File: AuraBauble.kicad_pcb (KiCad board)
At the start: 2 copper layers, 15 x 19 mm, 36 parts, among them J1 Bauble-Expando!, J2 USB_A, J3 SWD, SW1 KXT 321 LHS, U1 ATSAMD11D14A-M, U2 LP5912-3.3DRV, U3 74LVC1G02SE-7, Y1 FC-135R

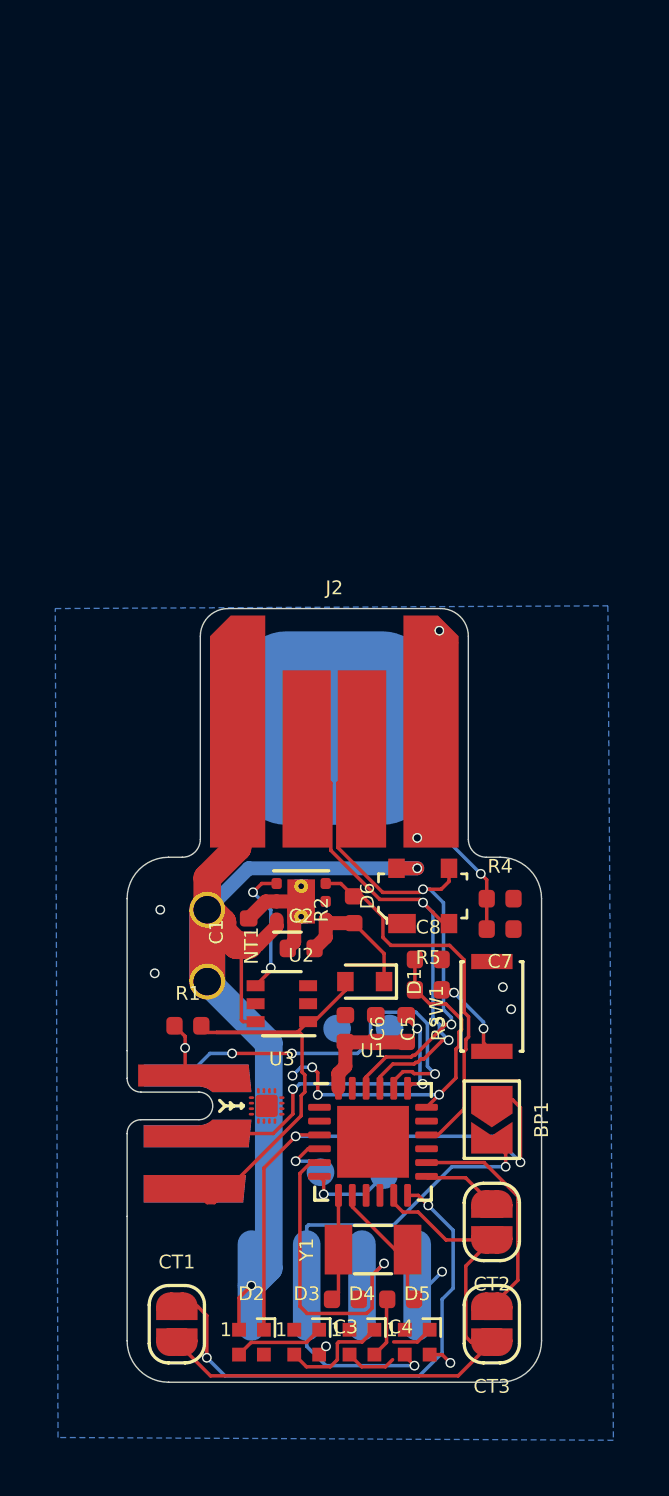
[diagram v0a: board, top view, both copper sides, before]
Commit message: Closing in on a rev0.
I still think I need to level shift the SPI signals to the LEDs.
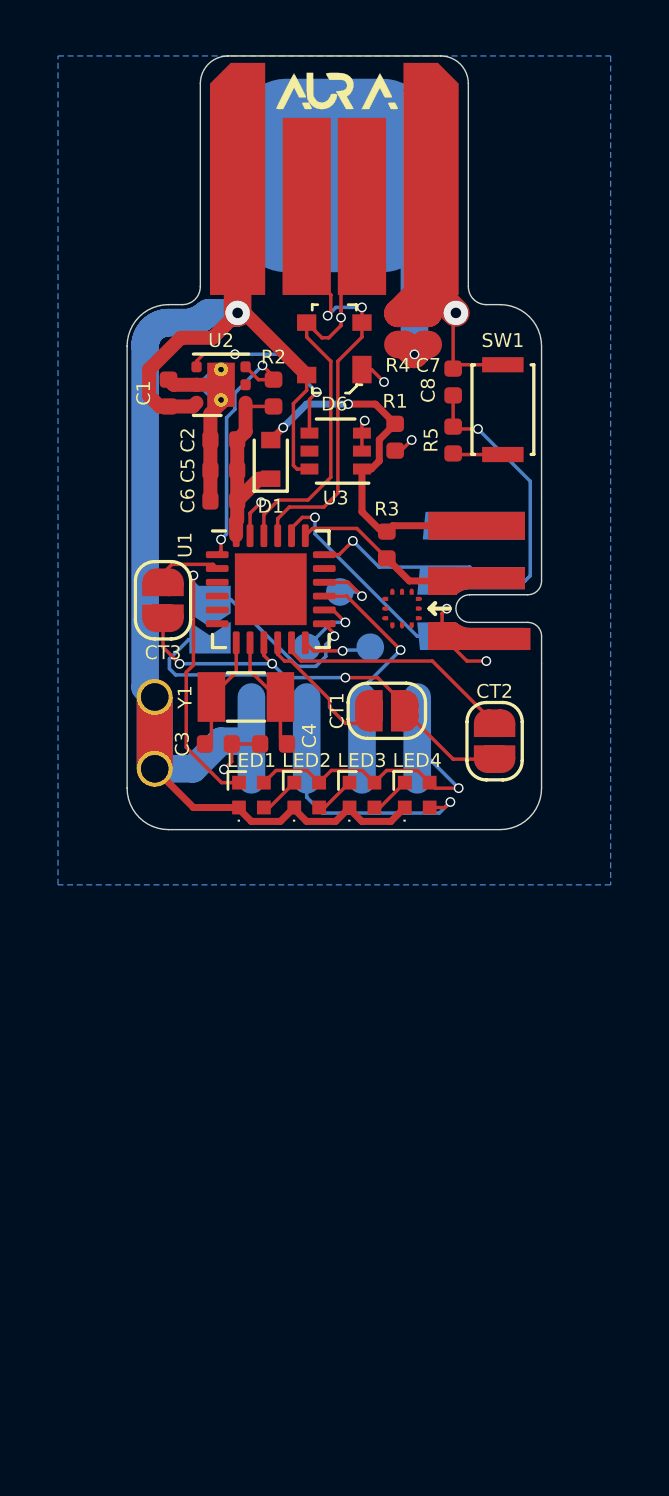
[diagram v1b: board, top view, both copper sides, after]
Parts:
- removed D2, D3, D4, D5: SK6805, LED_SMD:LED_SK6812_EC15_1.5x1.5mm
- removed TP4: TestPoint_Small, TestPoint:TestPoint_Pad_D1.0mm
- added LED1: SK6805, LED_SMD:LED_SK6812_EC15_1.5x1.5mm, F.Cu at (147.0, 76.8)
- added LED2: SK6805, LED_SMD:LED_SK6812_EC15_1.5x1.5mm, F.Cu at (149.0, 76.8)
- added LED3: SK6805, LED_SMD:LED_SK6812_EC15_1.5x1.5mm, F.Cu at (151.0, 76.8)
- added LED4: SK6805, LED_SMD:LED_SK6812_EC15_1.5x1.5mm, F.Cu at (153.0, 76.8)
- added REF**: AuraBauble_Wordmark, AuraBauble:AuraBauble_Wordmark, B.Cu at (151.3, 64.3)
- added REF**: AuraBable_Logo, AuraBauble:AuraBable_Logo, B.Cu at (151.3, 66.8)
- BP1: moved to B.Cu
- J3: footprint Connector_DebugEdge:DebugEdge_2x05_Target -> Connector_DebugEdge:DebugEdge_2x03_Target
- moved CT3 28.8 mm to (143.8, 69.7)
- moved J3 25.0 mm to (157.5, 69.0), turned to 90 degrees
- moved CT1 23.5 mm to (151.9, 73.7), turned to 0 degrees
- moved R1 22.6 mm to (152.2, 63.8), turned to 90 degrees
- moved C7 22.0 mm to (153.4, 59.8), turned to 270 degrees
- moved SW1 21.6 mm to (156.1, 62.8)
- moved R4 21.0 mm to (152.3, 59.8), turned to 90 degrees
- moved C5 20.9 mm to (146.0, 65.0), turned to 0 degrees
- moved C8 20.9 mm to (154.3, 61.8), turned to 90 degrees
- moved BP1 20.8 mm to (145.5, 70.4)
- moved C3 20.6 mm to (145.8, 74.9)
- moved C4 20.6 mm to (147.8, 74.9)
- moved Y1 20.5 mm to (146.8, 73.2)
- moved U1 20.3 mm to (147.7, 69.3)
- moved U3 20.1 mm to (150.1, 64.3)
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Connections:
- R3 pad 2: VCC -> +3V3
- TP3 pad 1: Net-(TP3-Pad1) -> /USB_SOF
- U1 pad 1: Net-(TP3-Pad1) -> /USB_POWER
- U1 pad 10: (no net) -> /TOUCH_Y_0
- U1 pad 11: /TOUCHX -> /TOUCH_Y_1
- U1 pad 12: /TOUCH_Y_0 -> /~SS~
- U1 pad 13: /TOUCH_Y_1 -> /MOSI
- U1 pad 14: /TOUCH_Y_2 -> /MISO
- U1 pad 15: (no net) -> /SCK
- U1 pad 16: /USB_POWER -> /USB_SOF
- U1 pad 2: Net-(TP4-Pad1) -> /TOUCH_Y_2
- U1 pad 3: /MOSI -> (no net)
- U1 pad 4: /MISO -> (no net)
- U1 pad 5: /SCK -> (no net)
- U1 pad 6: /~SS~ -> (no net)
- U1 pad 9: (no net) -> /TOUCHX
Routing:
- net GND: track 10.7 -> 47.6 mm, vias 10 -> 9
- net /TOUCH_Y_0: track 18.7 -> 5.11 mm, vias 2 -> 0
- net VBUS: track 22.5 -> 35.6 mm
- net /SWCLK: track 12.9 -> 5.85 mm, vias 3 -> 0
- net /TOUCH_Y_1: track 2.78 -> 8.74 mm
- net /TOUCHX: track 21.7 -> 15.8 mm, vias 0 -> 3
- net /TOUCH_Y_2: track 8.18 -> 2.48 mm
- net /SWDIO: track 14.2 -> 9.52 mm, vias 3 -> 1
- net /USB_POWER: track 13.9 -> 9.41 mm, vias 0 -> 2
- net +3V3: track 17.8 -> 13.7 mm, vias 0 -> 2
- net /SCK: track 11.4 -> 7.35 mm
- net Net-(D3-Pad2): track 3.99 -> 0.00 mm
- net Net-(D4-Pad2): track 3.33 -> 0.00 mm
- net /MOSI: track 20.0 -> 16.7 mm
- net Net-(D2-Pad2): track 3.27 -> 0.00 mm
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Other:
- outline, holes or cut-outs redrawn
- board text added: "cmd.wtf rev0"

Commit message: Crammed a level shifter in, added fifth LED.
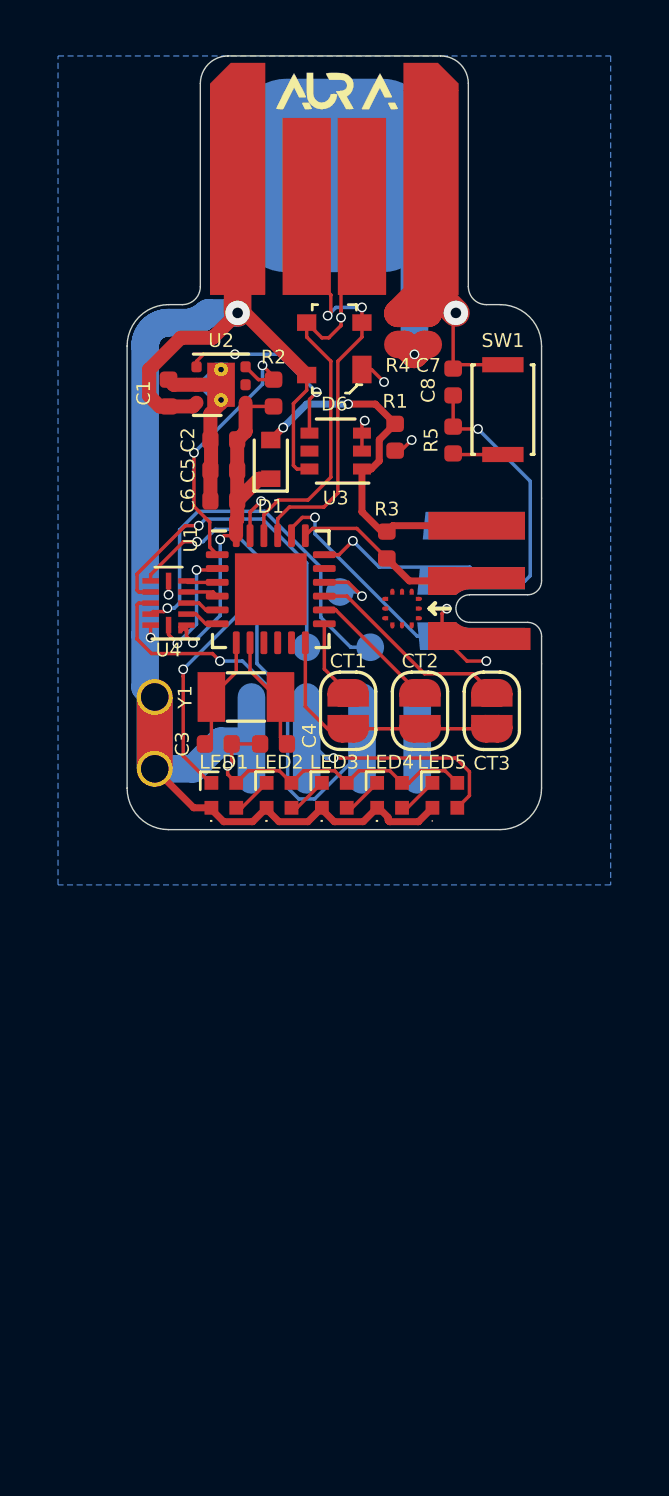
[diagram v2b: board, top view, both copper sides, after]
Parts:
- added LED5: SK6805, LED_SMD:LED_SK6812_EC15_1.5x1.5mm, F.Cu at (154.0, 76.8)
- added U4: NXB0104GU12X, AuraBauble:XQFN12, F.Cu at (144.0, 69.8)
- moved CT3 12.6 mm to (155.7, 73.7)
- moved CT2 2.92 mm to (153.1, 73.7)
- moved BP1 2.46 mm to (147.7, 69.3)
- moved CT1 1.40 mm to (150.5, 73.7), turned to 270 degrees
- moved LED1 1.00 mm to (146.0, 76.8)
- moved LED2 1.00 mm to (148.0, 76.8)
- moved LED3 1.00 mm to (150.0, 76.8)
- moved LED4 1.00 mm to (152.0, 76.8)
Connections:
- BP1 pad 1: /MOSI -> /MOSI_5V
- J1 pad 3: /SCK -> /SCK_5V
- LED1 pad 4: /MOSI -> /MOSI_5V
- LED4 pad 2: Net-(BP1-Pad2) -> Net-(LED4-Pad2)
- TP1 pad 1: /MISO -> /MISO_5V
- TP2 pad 1: /~SS~ -> /~CS_5V~
- U1 pad 10: /TOUCH_Y_0 -> (no net)
- U1 pad 11: /TOUCH_Y_1 -> (no net)
- U1 pad 12: /~SS~ -> /TOUCHX
- U1 pad 13: /MOSI -> /TOUCH_Y_0
- U1 pad 14: /MISO -> /TOUCH_Y_1
- U1 pad 15: /SCK -> /TOUCH_Y_2
- U1 pad 2: /TOUCH_Y_2 -> /SPI_5V_EN
- U1 pad 3: (no net) -> /MOSI
- U1 pad 4: (no net) -> /MISO
- U1 pad 5: (no net) -> /SCK
- U1 pad 6: (no net) -> /~CS~
- U1 pad 9: /TOUCHX -> (no net)
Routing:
- net /MOSI_5V: track 0.00 -> 15.8 mm, vias 0 -> 2
- net /MOSI: track 16.7 -> 1.13 mm, vias 2 -> 0
- net /SCK_5V: track 0.00 -> 15.2 mm, vias 0 -> 1
- net /~CS_5V~: track 0.00 -> 14.1 mm, vias 0 -> 1
- net /MISO_5V: track 0.00 -> 11.8 mm, vias 0 -> 1
- net /TOUCHX: track 15.8 -> 9.39 mm, vias 3 -> 0
- net /SCK: track 7.35 -> 1.22 mm, vias 1 -> 0
- net VCC: track 7.57 -> 13.7 mm, vias 0 -> 2
- net /TOUCH_Y_2: track 2.48 -> 7.51 mm
- net /SPI_5V_EN: track 0.00 -> 4.51 mm, vias 0 -> 2
- net /TOUCH_Y_1: track 8.74 -> 4.71 mm
- net Net-(BP1-Pad2): track 17.9 -> 14.1 mm
- net /~SS~: track 2.48 -> 0.00 mm, vias 1 -> 0
- net /TOUCH_Y_0: track 5.11 -> 2.86 mm
- net /MISO: track 2.72 -> 1.17 mm, vias 1 -> 0
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
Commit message: 3d Shapes!
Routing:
- net GND: track 47.5 -> 48.7 mm, vias 9 -> 30

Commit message: Update some annotations.
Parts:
- renumbered D6 to D2

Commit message: Somebody had SWDIO/SWCLK swapped.
It's me. I'm somebody.
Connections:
- J3 pad 2: /SWCLK -> /SWDIO
- J3 pad 3: /SWDIO -> /SWCLK
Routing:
- net /SWCLK: track 5.85 -> 8.53 mm, vias 0 -> 1
- net /SWDIO: track 9.52 -> 7.50 mm, vias 1 -> 2
- net GND: vias 30 -> 27

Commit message: Cleanup.
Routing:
- net GND: vias 27 -> 30
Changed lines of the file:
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@@
     (thickness 1.6)
     (drawings 16)
-    (tracks 440)
+    (tracks 443)
     (zones 0)
     (modules 39)
@@
   (title_block
     (title "Aura Bauble")
-    (date 2020-09-13)
+    (date 2020-09-14)
     (rev 0)
     (company cmd.wtf)
+    (comment 1 "BYOBEL: Bring Your Own BlinkEnLights")
+    (comment 3 "addressable RGB LEDs.")
+    (comment 4 "Aura Bauble is a USB device that communicates with ASUS Aura software to control ")
   )
   (layers
@@
     (34 B.Paste user hide)
     (35 F.Paste user hide)
-    (36 B.SilkS user hide)
-    (37 F.SilkS user hide)
+    (36 B.SilkS user)
+    (37 F.SilkS user)
     (38 B.Mask user hide)
     (39 F.Mask user hide)
@@
   (via (at 147.9 59.4) (size 0.3556) (drill 0.254) (layers F.Cu B.Cu) (net 3))
   (via (at 148.2 71.95) (size 0.3556) (drill 0.254) (layers F.Cu B.Cu) (net 3))
+  (via (at 152.7 67.5) (size 0.3556) (drill 0.254) (layers F.Cu B.Cu) (net 3))
+  (via (at 150.1 66.5) (size 0.3556) (drill 0.254) (layers F.Cu B.Cu) (net 3))
+  (via (at 148.9 65.5) (size 0.3556) (drill 0.254) (layers F.Cu B.Cu) (net 3))
   (segment (start 144.8775 62.685) (end 145.0125 62.55) (width 0.508) (layer F.Cu) (net 4))
   (segment (start 144 62.685) (end 144.8775 62.685) (width 0.508) (layer F.Cu) (net 4))
